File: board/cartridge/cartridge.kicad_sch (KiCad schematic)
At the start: 36 parts, among them J1 TF-115-BCP9, J2 HC-TYPE-C-16P-01B, Q1 DMG2301L, SW1 K3-1410S, SW2 K3-1410S, U1 AMS1117-3.3, U10 TPS2041B, U11 LM66100DCK, U12 LM66100DCK, U2 ESP32-S3-WROOM-1U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

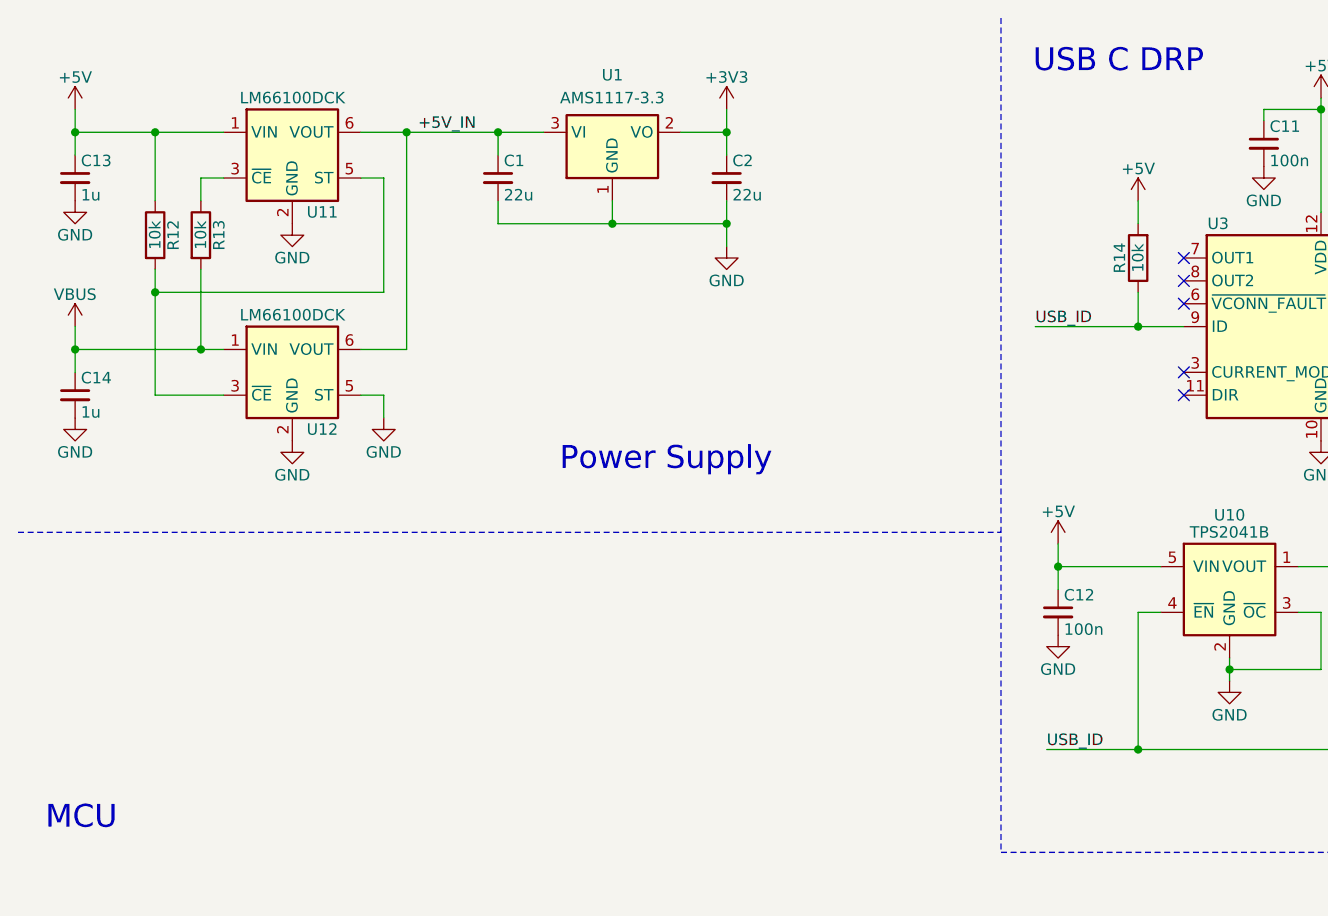
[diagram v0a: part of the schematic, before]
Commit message: Finish USB power management.
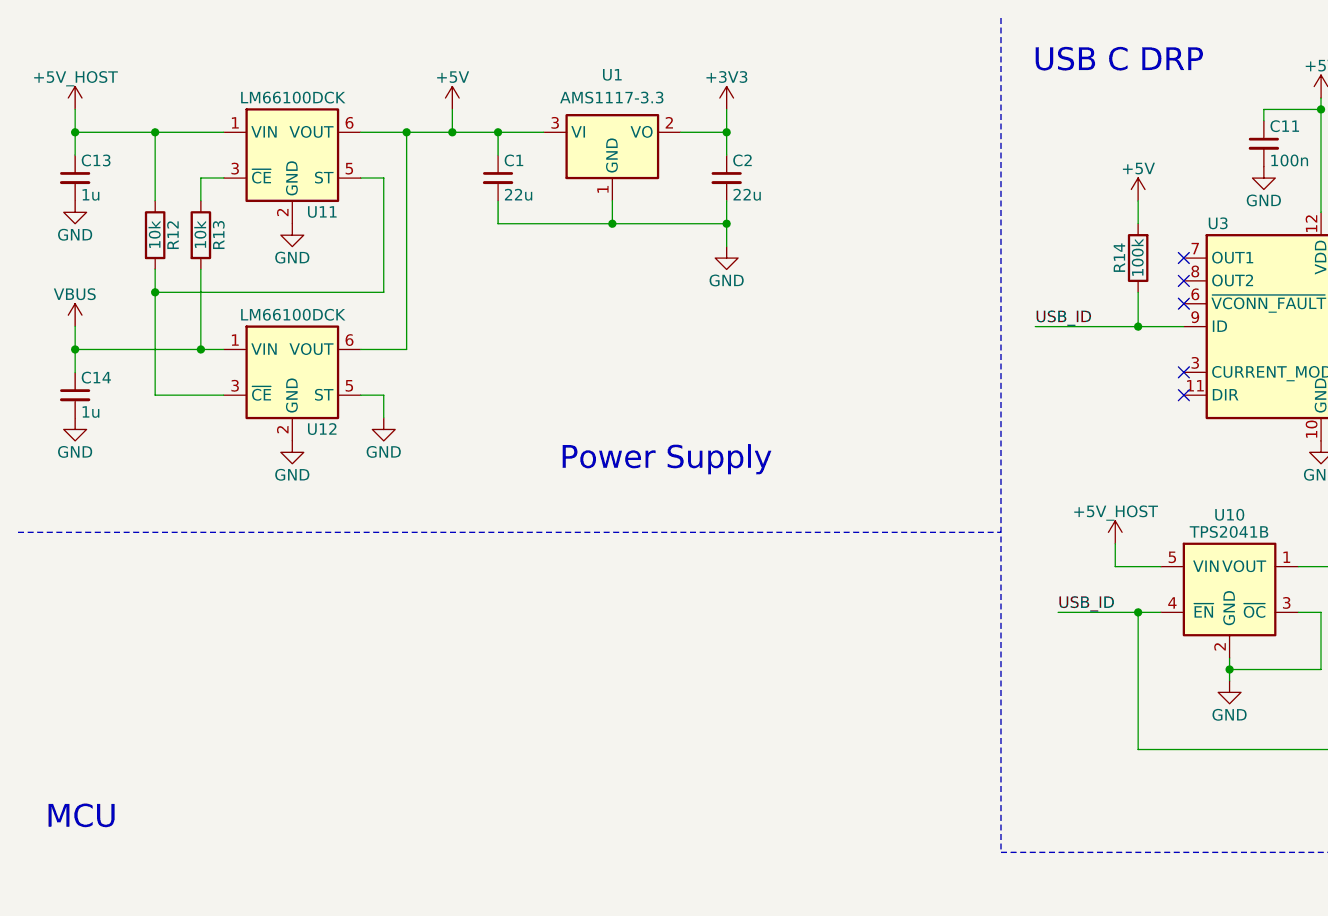
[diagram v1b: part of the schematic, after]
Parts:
- removed C12: 100n, Capacitor_SMD:C_0603_1608Metric, symbol Device:C_Small
- C16: footprint Capacitor_SMD:CP_Elec_6.3x7.7 -> Capacitor_Tantalum_SMD:CP_EIA-3528-21_Kemet-B
- Q1: footprint Package_TO_SOT_SMD:SOT-23 -> 0Project:SOT-23
- R14: value 10k -> 100k
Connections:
- net +5V_IN is gone; now on net +5V: C1.1, U1.3 (VI), U11.6 (VOUT), U12.6 (VOUT)
- net +5V: no longer C13.1, R12.1, U10.5 (VIN), U11.1 (VIN)
- new net +5V_HOST: C13.1, R12.1, U10.5 (VIN), U11.1 (VIN)

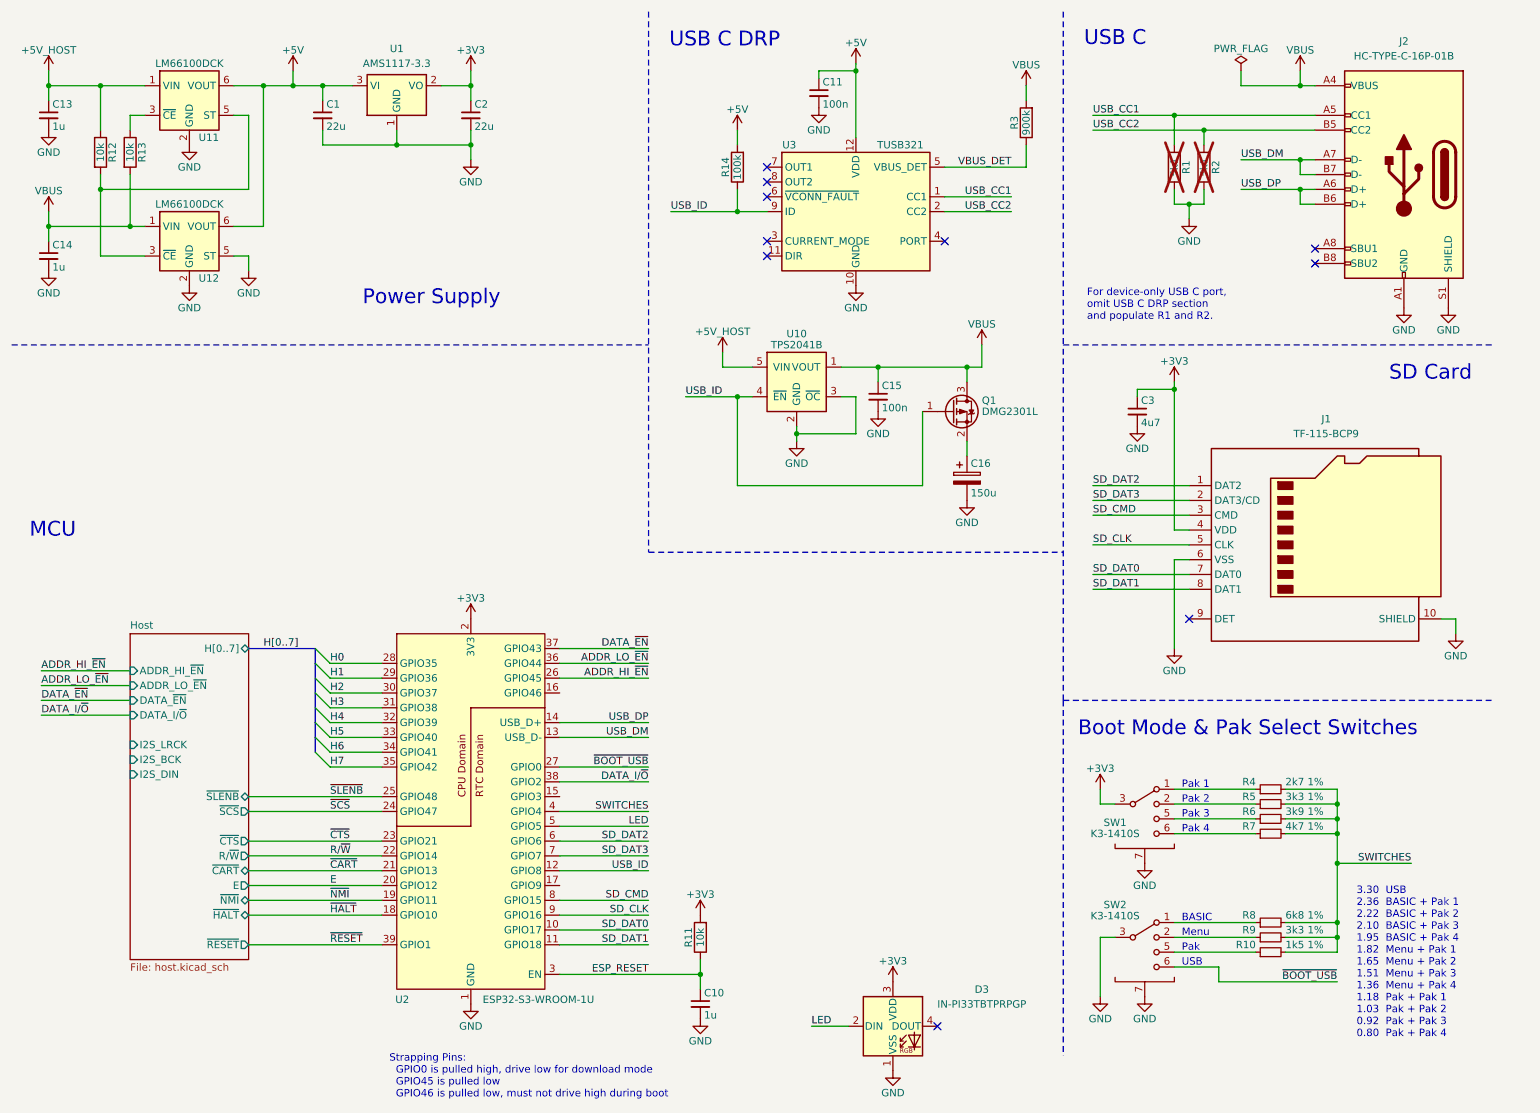
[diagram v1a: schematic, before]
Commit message: Add 32 kHz crystal.
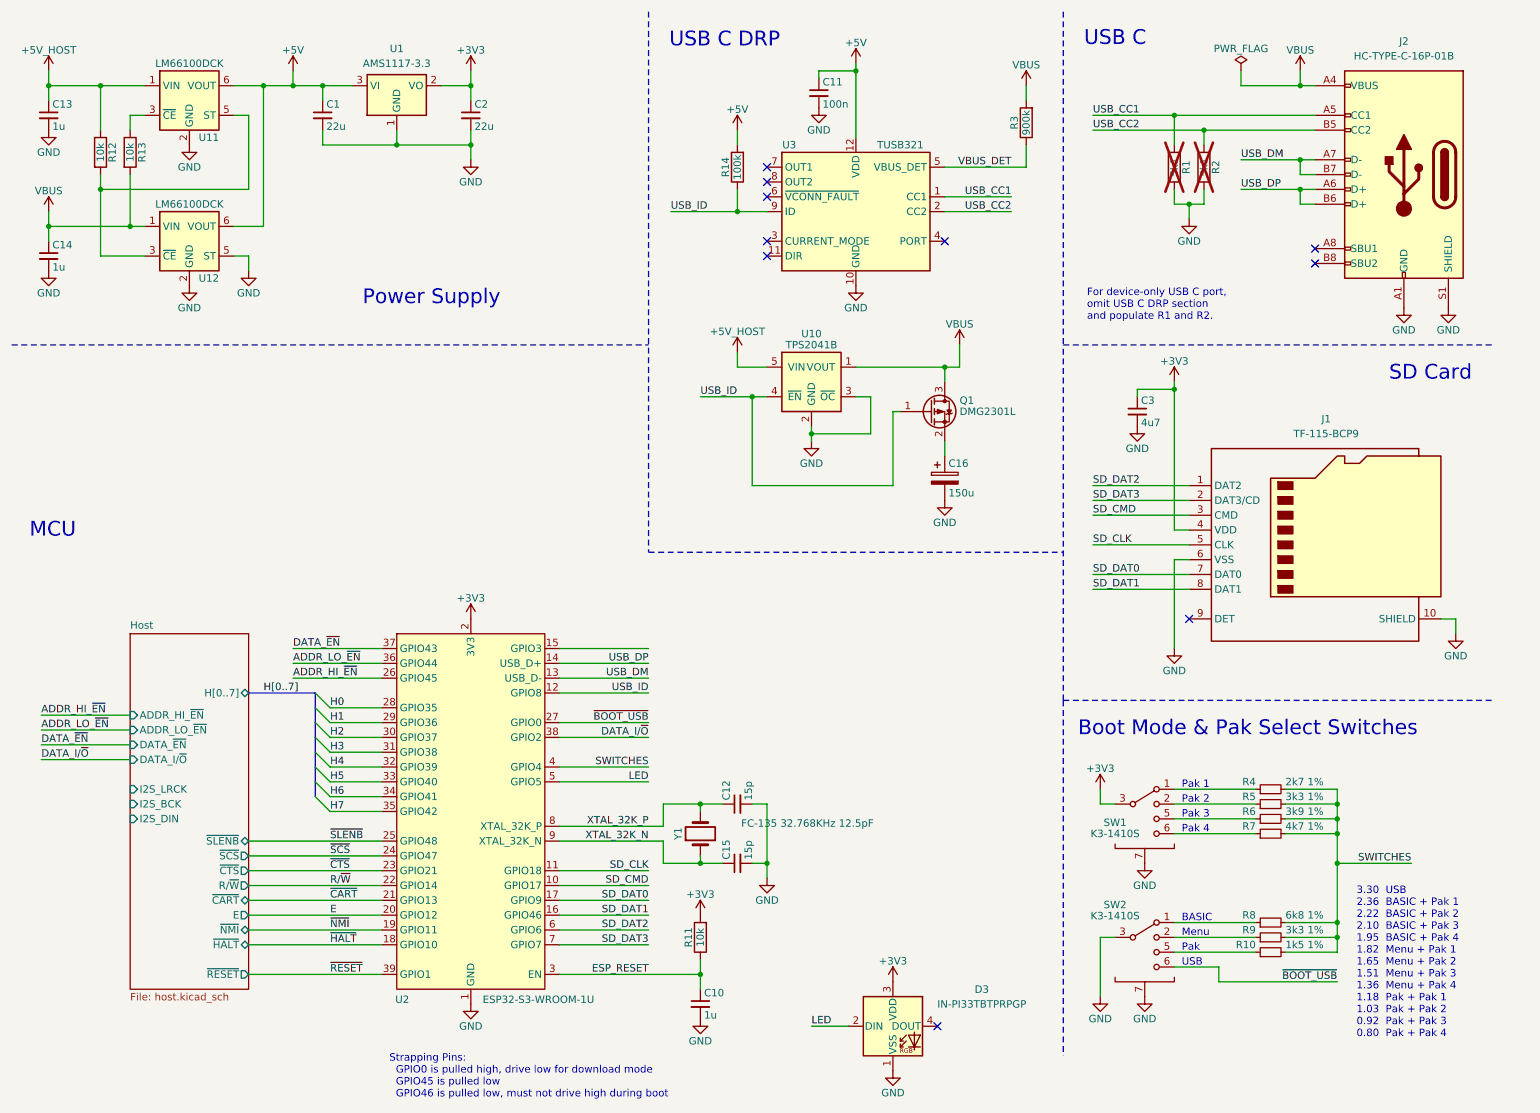
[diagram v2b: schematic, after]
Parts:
- added C12: 15p, Capacitor_SMD:C_0603_1608Metric, symbol Device:C_Small
- added Y1: FC-135 32.768KHz 12.5pF, Crystal:Crystal_SMD_3215-2Pin_3.2x1.5mm, symbol Device:Crystal
- C15: value 100n -> 15p
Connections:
- net GND: now also C12.2
- net SD_CLK: now also U2.11 (GPIO18); no longer U2.9 (GPIO16)
- net SD_CMD: now also U2.10 (GPIO17); no longer U2.8 (GPIO15)
- net SD_DAT0: now also U2.17 (GPIO9); no longer U2.10 (GPIO17)
- net SD_DAT1: now also U2.16 (GPIO46); no longer U2.11 (GPIO18)
- net VBUS: no longer C15.1
- new net XTAL_32K_N: C15.1, U2.9 (XTAL_32K_N), Y1.1
- new net XTAL_32K_P: C12.1, U2.8 (XTAL_32K_P), Y1.2
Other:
- moved on the sheet: C16, Q1, U10

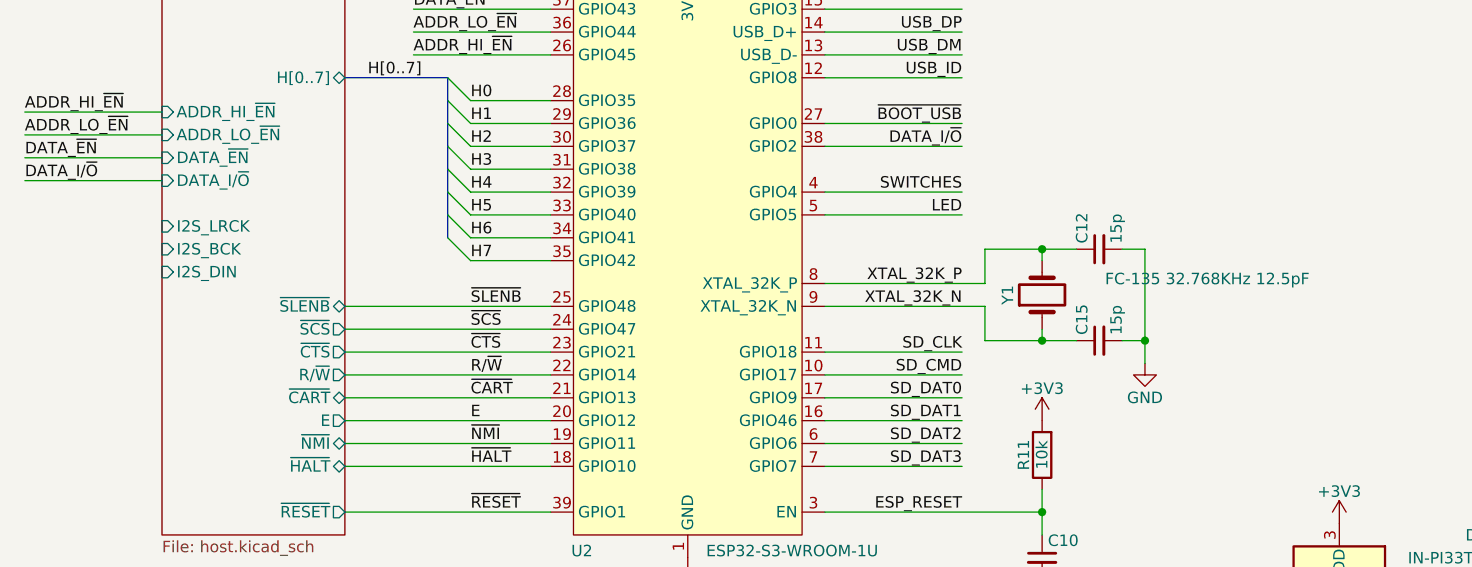
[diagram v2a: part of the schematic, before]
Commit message: Remove watch crystal and audio DAC.
These can be implemented later; they're not needed
for a first-gen prototype to determine whether the
ESP32-S3 will even be able to bit-bang the bus.
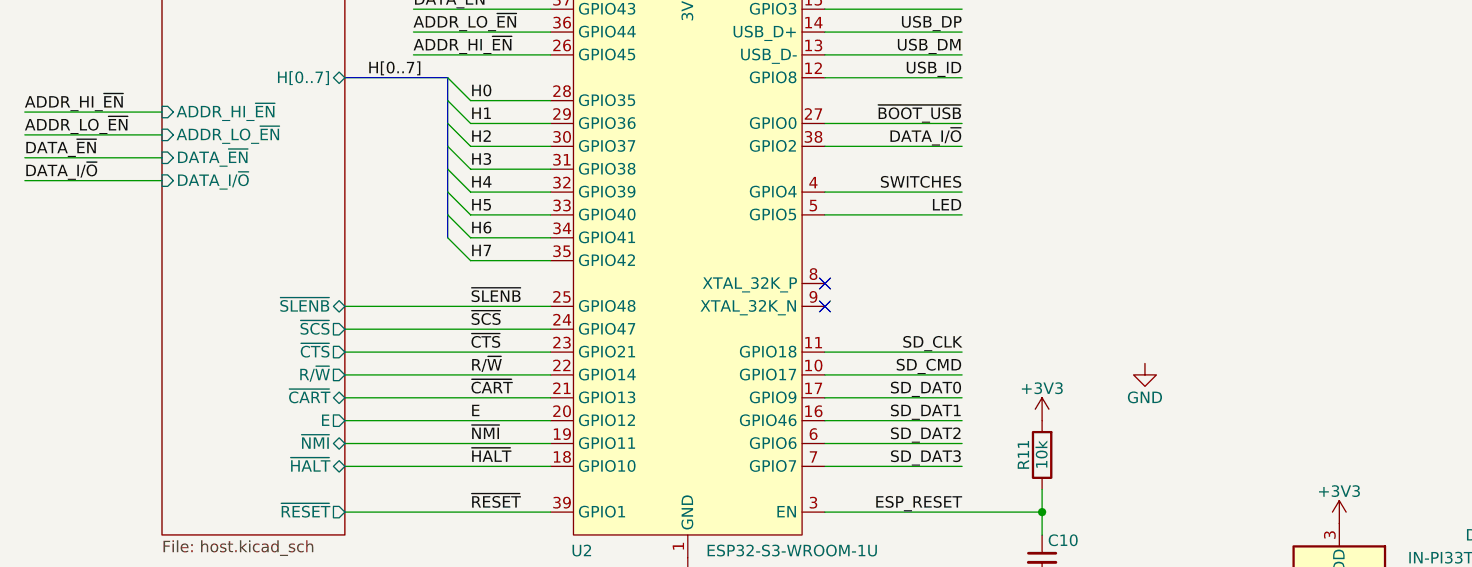
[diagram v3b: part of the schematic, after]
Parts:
- removed C12, C15: 15p, Capacitor_SMD:C_0603_1608Metric, symbol Device:C_Small
- removed Y1: FC-135 32.768KHz 12.5pF, Crystal:Crystal_SMD_3215-2Pin_3.2x1.5mm, symbol Device:Crystal
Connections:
- net XTAL_32K_N: no longer names the net of U2.9 (XTAL_32K_N)
- net XTAL_32K_P: no longer names the net of U2.8 (XTAL_32K_P)
- no-connect marks 10 -> 12
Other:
- sheet Host ports: added none; removed I2S_BCK, I2S_DIN, I2S_LRCK
